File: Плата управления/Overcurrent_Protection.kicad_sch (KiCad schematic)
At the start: 15 parts, among them U1 LMV7239M5, U7 AD8210, U8 LMV324

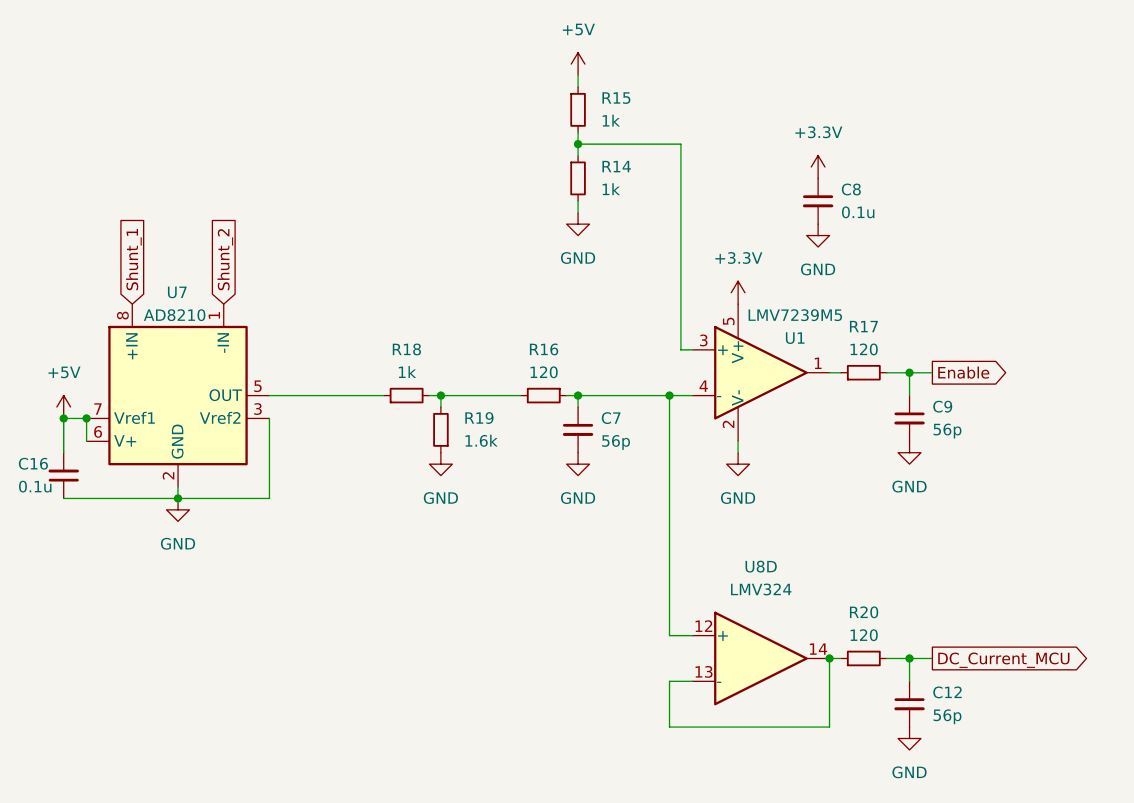
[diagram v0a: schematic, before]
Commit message: Добавил питание MCU и кварц на 8Мгц
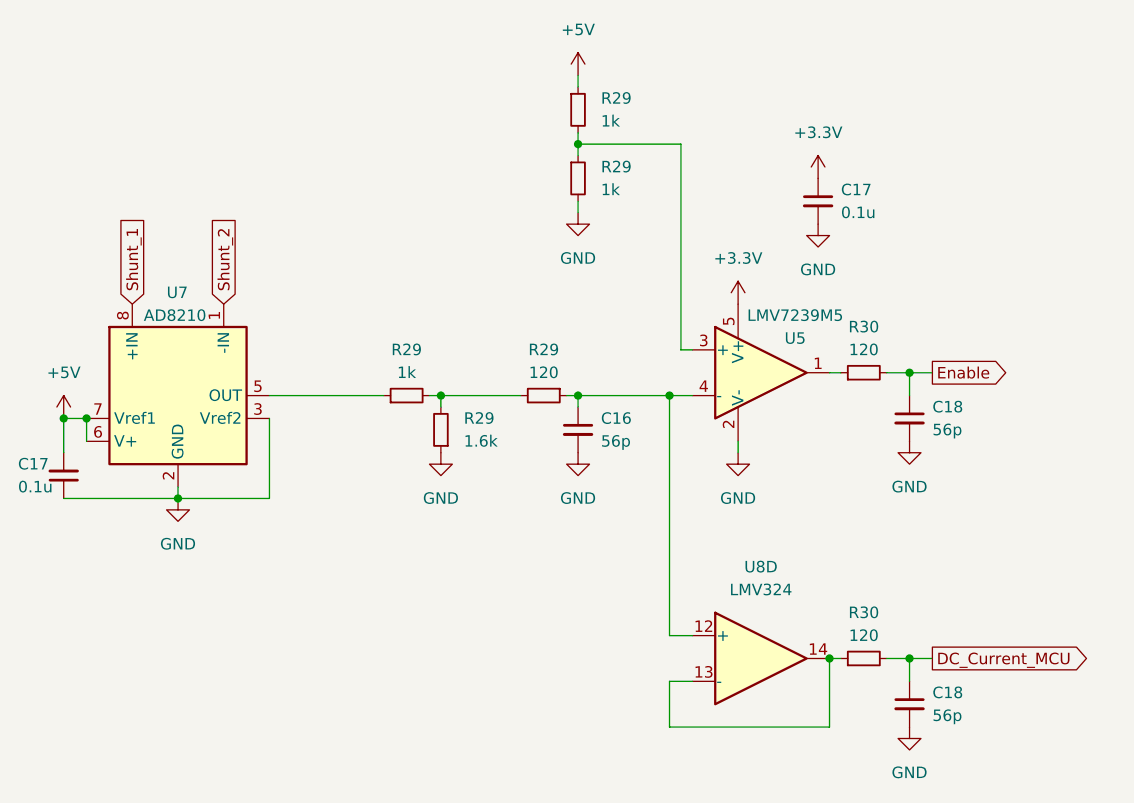
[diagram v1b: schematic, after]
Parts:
- renumbered C7 to C16, C8 to C17, C16 to C17, C9 to C18, C12 to C18, R15 to R29, R14 to R29, R16 to R29, R18 to R29, R19 to R29, R20 to R30, R17 to R30, U1 to U5

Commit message: Привел в порядок схему
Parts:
- removed C17: 0.1u, Capacitor_SMD:C_0603_1608Metric_Pad1.08x0.95mm_HandSolder, symbol Device:C_Small
- removed C18: 56p, Capacitor_SMD:C_0603_1608Metric_Pad1.08x0.95mm_HandSolder, symbol Device:C_Small
- removed R29: 1k, Resistor_SMD:R_0603_1608Metric_Pad0.98x0.95mm_HandSolder, symbol Device:R_Small
- removed R29: 1.6k, Resistor_SMD:R_0603_1608Metric_Pad0.98x0.95mm_HandSolder, symbol Device:R_Small
- removed R30: 120, Resistor_SMD:R_0603_1608Metric_Pad0.98x0.95mm_HandSolder, symbol Device:R_Small
- removed U7: AD8210, Package_SO:SOIC-8_3.9x4.9mm_P1.27mm, symbol Amplifier_Current:AD8210
- removed U8: LMV324, symbol Amplifier_Operational:LMV324
- added C16: 0.1u, Capacitor_SMD:C_0603_1608Metric_Pad1.08x0.95mm_HandSolder, symbol Device:C_Small
- added U5: INA283, Package_SO:SOIC-8_3.9x4.9mm_P1.27mm, symbol Amplifier_Current:INA283
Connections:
- net +5V is gone; now on net +3.3V: R29.1
- net +3.3V: now also C16.1, U5.3 (REF2), U5.6 (V+)
- net GND: now also C16.2, U5.2 (GND), U5.7 (REF1)
- net Shunt_1: now also U5.1 (-)
- net Shunt_2: now also U5.8 (+)
- net at R29.2: now also U5.5
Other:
- moved on the sheet: C16, C17, C18, R29, R30, U5

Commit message: Расставил драйвера
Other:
- note added: "Защита от КЗ"
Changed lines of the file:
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@@
     (fill (type none))
+  )
+  (text "Защита от КЗ" (at 19.05 20.32 0)
+    (effects (font (size 2 2) bold) (justify left bottom))
   )
   (global_label "Shunt_1" (shape input) (at 30.48 64.77 180) (fields_autoplaced)

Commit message: Редактировал схему
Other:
- note added: "Уставка по току"
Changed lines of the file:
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@@
     (fill (type none))
+  )
+  (rectangle (start 46.99 19.05) (end 69.85 48.26)
+    (stroke (width 0) (type dot))
+    (fill (type none))
+  )
+  (text "Уставка\nпо току" (at 48.26 24.13 0)
+    (effects (font (size 1.27 1.27)) (justify left bottom))
   )
   (text "Защита от КЗ" (at 19.05 20.32 0)

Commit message: Ещё нужно доработать
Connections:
- net at R29.1, R29.2: now also U5.4 (-); no longer U5.3 (+)
- net at C16.1, R29.1: now also U5.3 (+); no longer U5.4 (-)
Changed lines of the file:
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@@
 (kicad_sch (version 20230121) (generator eeschema)
   (paper "A4")
+  (junction (at 97.79 59.69) (diameter 0) (color 0 0 0 0)
+  )
   (junction (at 60.96 62.23) (diameter 0) (color 0 0 0 0)
-  )
-  (junction (at 97.79 59.69) (diameter 0) (color 0 0 0 0)
   )
   (junction (at 60.96 34.29) (diameter 0) (color 0 0 0 0)
@@
     (stroke (width 0) (type default))
   )
-  (wire (pts (xy 72.39 57.15) (xy 72.39 34.29))
+  (wire (pts (xy 68.58 62.23) (xy 68.58 34.29))
     (stroke (width 0) (type default))
   )
@@
     (stroke (width 0) (type default))
   )
-  (wire (pts (xy 72.39 34.29) (xy 60.96 34.29))
-    (stroke (width 0) (type default))
-  )
   (wire (pts (xy 60.96 71.12) (xy 60.96 68.58))
     (stroke (width 0) (type default))
@@
     (stroke (width 0) (type default))
   )
-  (wire (pts (xy 73.66 57.15) (xy 72.39 57.15))
+  (wire (pts (xy 60.96 57.15) (xy 73.66 57.15))
     (stroke (width 0) (type default))
   )
@@
     (stroke (width 0) (type default))
   )
-  (wire (pts (xy 60.96 62.23) (xy 73.66 62.23))
-    (stroke (width 0) (type default))
-  )
   (wire (pts (xy 60.96 40.64) (xy 60.96 41.91))
     (stroke (width 0) (type default))
@@
     (stroke (width 0) (type default))
   )
+  (wire (pts (xy 73.66 62.23) (xy 68.58 62.23))
+    (stroke (width 0) (type default))
+  )
+  (wire (pts (xy 68.58 34.29) (xy 60.96 34.29))
+    (stroke (width 0) (type default))
+  )
+  (wire (pts (xy 60.96 57.15) (xy 60.96 62.23))
+    (stroke (width 0) (type default))
+  )

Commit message: Добавил документы
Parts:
- R29: value 1k -> 1.3k
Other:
- moved on the sheet: C16, C17, C18, R29, R30, U5

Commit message: Версия под отчёт
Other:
- note removed: "Уставка по току"
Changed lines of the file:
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@@
     (fill (type none))
   )
-  (rectangle (start 137.795 67.31) (end 160.655 96.52)
-    (stroke (width 0) (type dot))
-    (fill (type none))
-  )
-  (text "Уставка\nпо току" (at 139.065 72.39 0)
-    (effects (font (size 1.27 1.27)) (justify left bottom))
-  )
   (text "Защита от КЗ" (at 146.685 62.23 0)
-    (effects (font (size 2 2) bold) (justify left bottom))
+    (effects (font (size 2.5 2.5) bold) (justify left bottom))
   )
   (global_label "Shunt_1" (shape input) (at 121.285 113.03 180) (fields_autoplaced)
